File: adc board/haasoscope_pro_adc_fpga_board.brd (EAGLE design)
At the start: 224.5 x 160 mm, 573 parts, among them CN2 12Vin, IC1 ADC12DL2500ACF, IC10 TPS72325DBVR, IC13 LMH5401IRMST, IC14 LMH6401IRMZR, IC15 SN74AVC4T774PWR, IC17 DAC8562SDGSR, IC18 TLV9102IPWR, IC2 SN74AVC4T774PWR, IC21 LMH5401IRMST, IC22 TPS7A7200RGTR, IC23 TPS7A7200RGTR, IC24 TPS7A7200RGTR, IC25 TPS72325DBVR, IC26 TPS7A7200RGTR, IC27 TPS7A7200RGTR, IC28 TPS7A7200RGTR, IC29 LMH6401IRMZR, IC3 ADC122S021CIMM_NOPB, IC30 SN74AVC4T774PWR, IC33 TLV9102IPWR, IC4 TLV9102IPWR, IC5 EP4CE30F23C6N, IC6 EPCQ16ASI8N, IC7 TPS7A7200RGTR, IC8 FT232HQ, IC9 93LC56B, J1 2p-2.54, J10 8pin, J11 8pin, J13 8pin, J14 2x5, J15 test1, J2 test1, J3 2p-2.54, J30 2p-2.54, J31 2p-2.54, J32 2p-2.54, J33 2p-2.54, J34 2p-2.54, J35 2p-2.54, J36 2p-2.54, J37 2p-2.54, J39 2p-2.54, J4 2p-2.54, J40 2p-2.54, J41 2p-2.54, J42 2p-2.54, J43 2p-2.54, J44 2p-2.54, J45 2p-2.54, J46 2p-2.54, J8 8pin, K1 G6K-2F-RF-T-TR03_DC5, K2 G6K-2F-RF-T-TR03_DC5, K3 G6K-2F-RF-T-TR03_DC5, K4 G6K-2F-RF-T-TR03_DC5, K5 G6K-2F-RF-T-TR03_DC5, K6 TLP3475R_TP,F, K7 TLP3475R_TP,F, Q1 S8050, Q4 S8050, Q5 S8050, Q7 S8050, Q8 S8050, Q9 S8050, SW3 SKQGADE010, SW4 SKQGADE010, U2 ADF4350BCPZ, X1 USBC, Y2 OSCILLATORSMD-5X3, Y3 12MHz

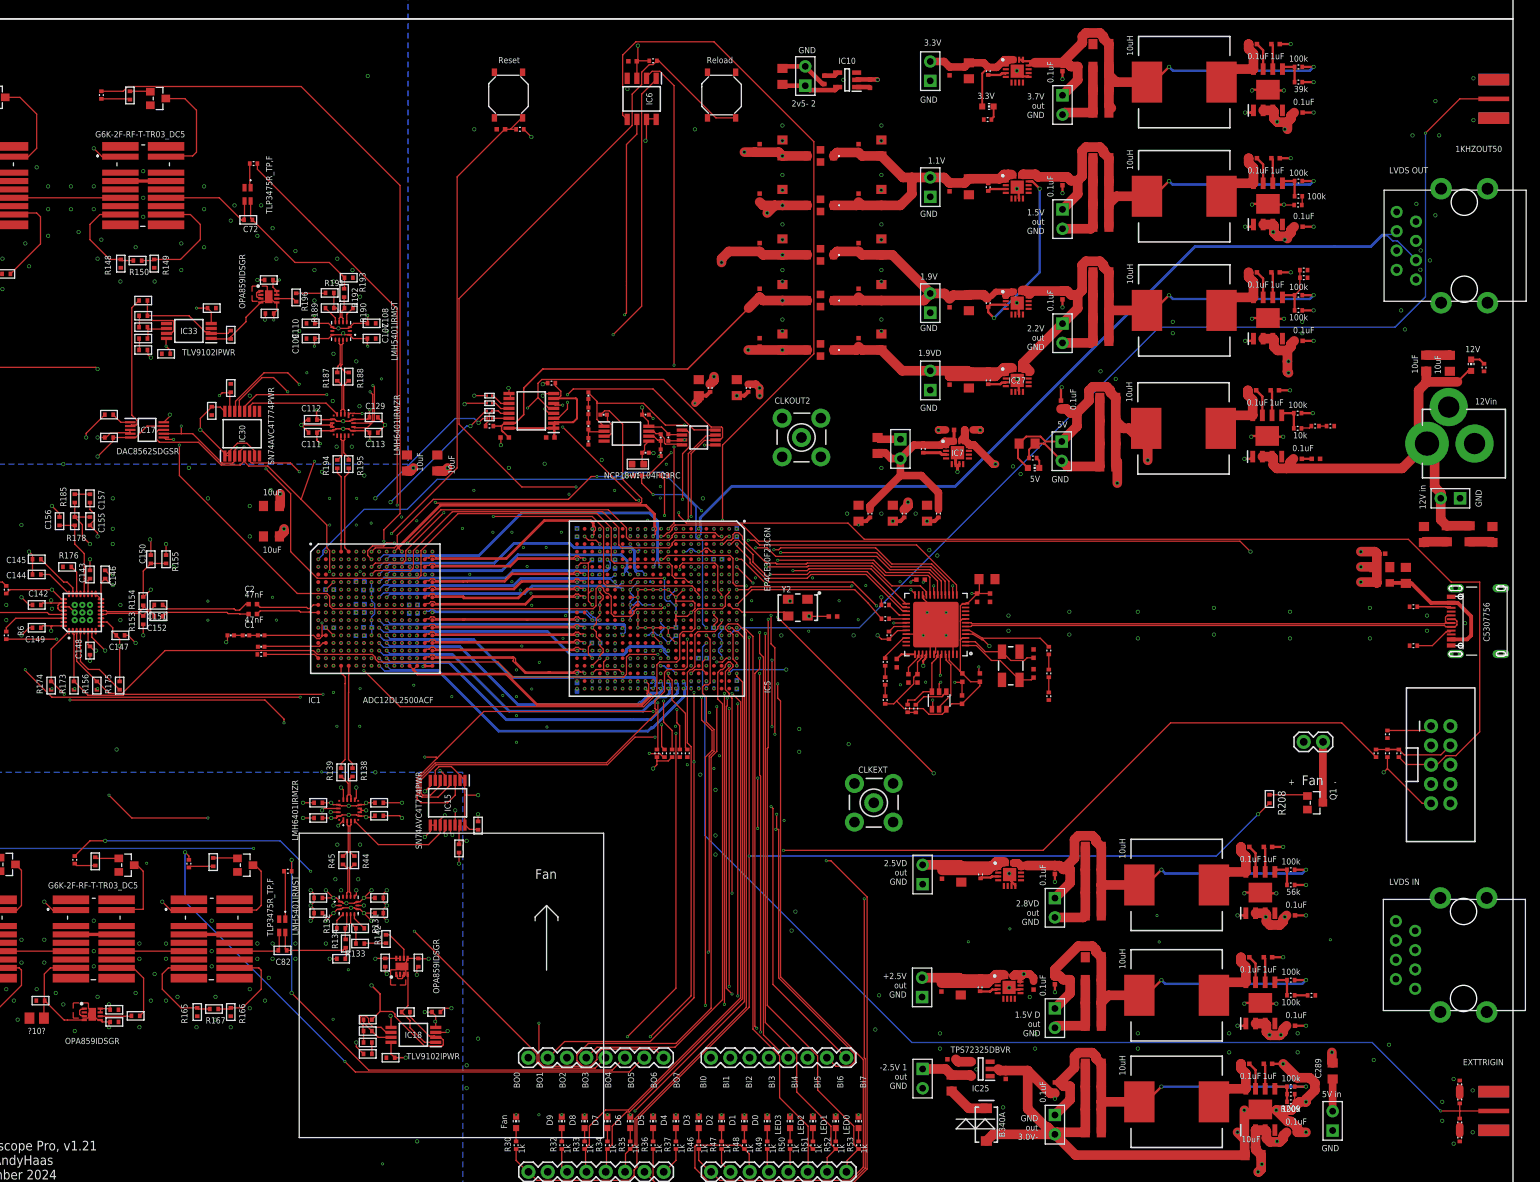
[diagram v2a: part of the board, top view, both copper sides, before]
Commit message: add more lables
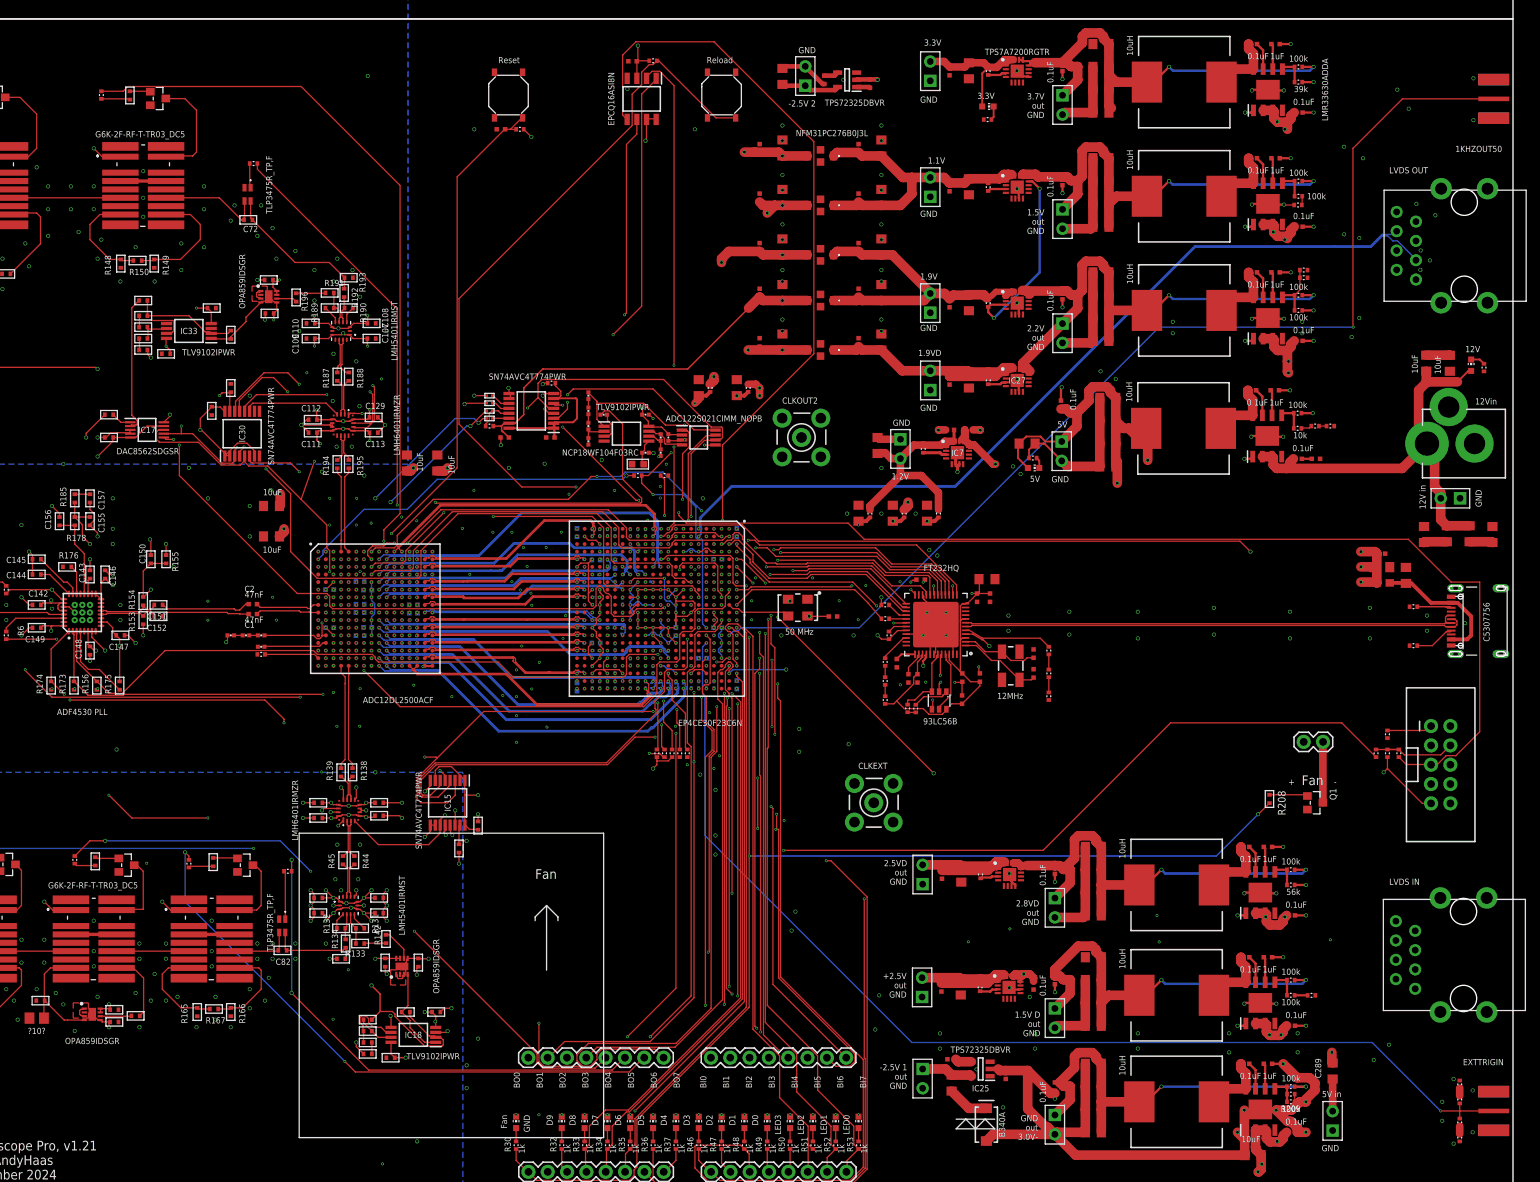
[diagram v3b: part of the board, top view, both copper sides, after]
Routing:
- net 1KHZOUT50: track 142.3 -> 143.5 mm
- net GND: vias 614 -> 617
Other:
- board text added: "-2.5V 2"
- board text added: "1.2V"
- board text added: "50 MHz"
- board text added: "ADF4530 PLL"
- board text removed: "2v5- 2"

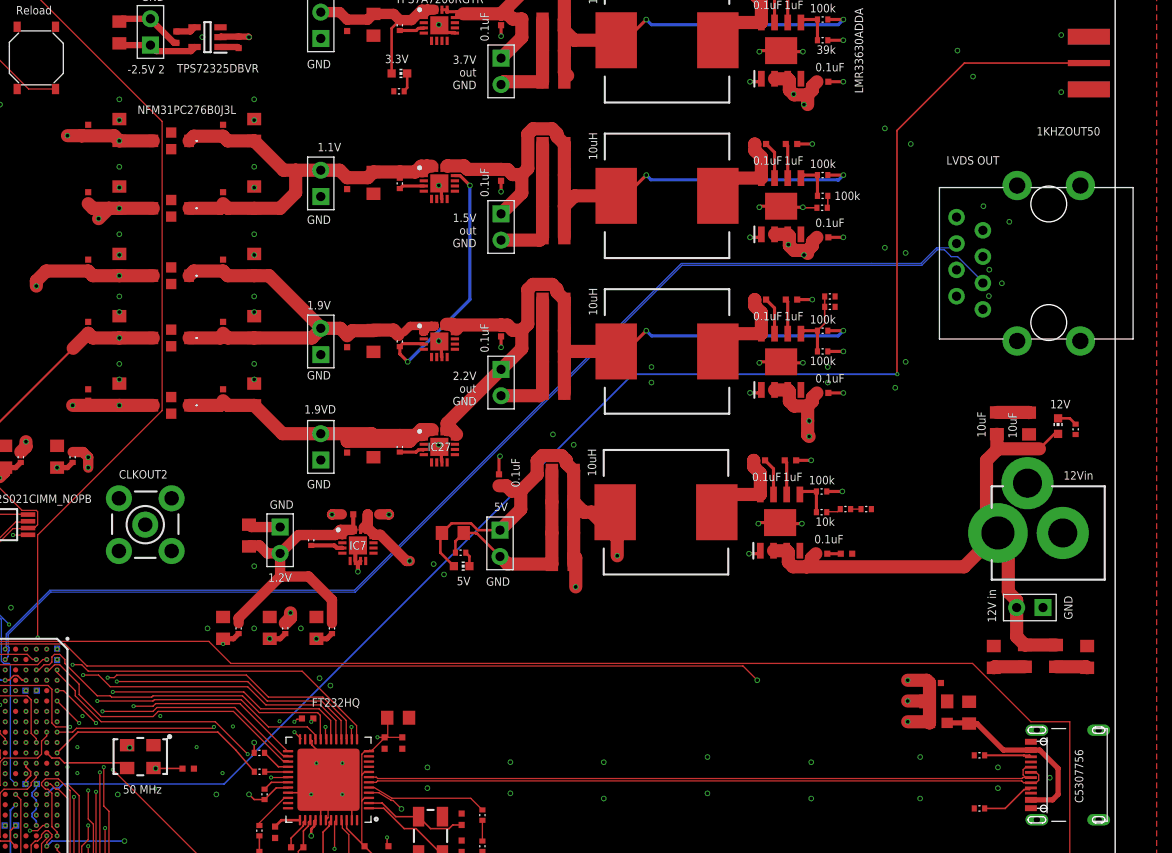
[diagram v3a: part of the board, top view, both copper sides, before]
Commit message: Add a resistor on the 50 ohm aux out line
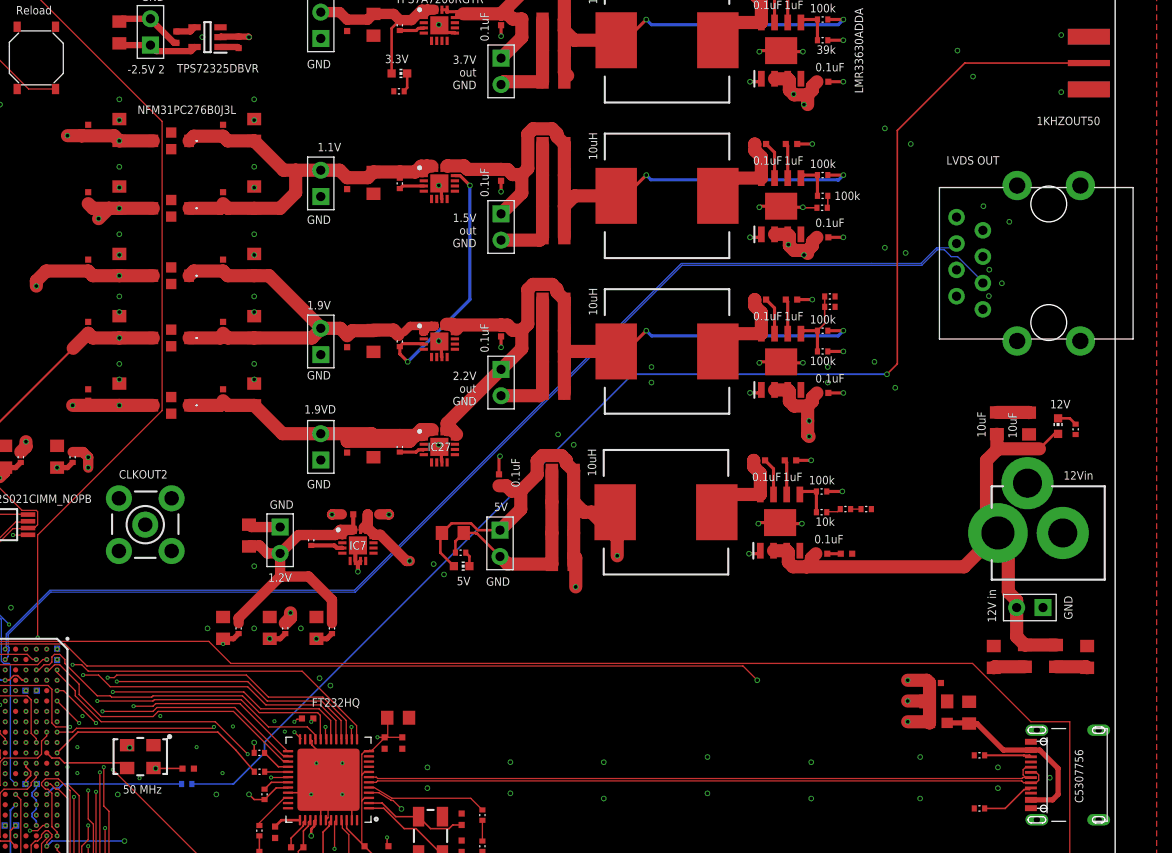
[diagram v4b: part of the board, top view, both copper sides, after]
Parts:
- added R211: 47, FlashPCB_Resistors:RES-0402
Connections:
- new net N$52: 1KHZOUT50.P, R211.P$1
- net 1KHZOUT50: now also R211.P$2; no longer 1KHZOUT50.P
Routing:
- net 1KHZOUT50: track 143.5 -> 13.4 mm, vias 2 -> 1
- net N$52: track 0.00 -> 129.0 mm, vias 0 -> 1
- net GND: vias 617 -> 618
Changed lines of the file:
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@@
 <drawing>
 <settings>
-<setting alwaysvectorfont="yes"/>
+<setting alwaysvectorfont="no"/>
 <setting verticaltext="up"/>
 </settings>
@@
 </element>
 <element name="1KHZOUT50" library="adafruit" package="SMA_EDGELAUNCH" value="50" x="224" y="146.5" smashed="yes" rot="R180">
-<attribute name="NAME" x="216.92" y="139.515" size="0.8128" layer="25"/>
+<attribute name="NAME" x="216.92" y="140.515" size="0.8128" layer="25"/>
+</element>
+<element name="R211" library="FlashPCB_Resistors" package="RES-0402" value="47" x="135" y="77" smashed="yes" rot="MR0">
+<attribute name="VALUE" x="135.77" y="78" size="0.8128" layer="22" font="vector" rot="MR0"/>
 </element>
 </elements>
@@
 <via x="135.95" y="80.55" extent="1-16" drill="0.2"/>
 <via x="138.45" y="78.05" extent="1-16" drill="0.2"/>
-<via x="131.95" y="76.55" extent="1-16" drill="0.2"/>
+<via x="130.45" y="77.55" extent="1-16" drill="0.2"/>
 <via x="139.45" y="82.55" extent="1-16" drill="0.2"/>
-<via x="143.95" y="83.05" extent="1-16" drill="0.2"/>
+<via x="143.45" y="83.05" extent="1-16" drill="0.2"/>
 <via x="24" y="125" extent="1-16" drill="0.2"/>
 <via x="24" y="122" extent="1-16" drill="0.2"/>
@@
 <via x="179.8" y="115.7" extent="1-16" drill="0.35"/>
 <via x="172.3" y="109.7" extent="1-16" drill="0.35"/>
-<via x="170.3" y="110.7" extent="1-16" drill="0.35"/>
+<via x="170.8" y="110.7" extent="1-16" drill="0.35"/>
 <via x="159.8" y="97.2" extent="1-16" drill="0.35"/>
 <via x="158.8" y="98.2" extent="1-16" drill="0.35"/>
@@
 <via x="202.3" y="128.7" extent="1-16" drill="0.35"/>
 <via x="204.3" y="128.2" extent="1-16" drill="0.35"/>
-<via x="204.3" y="117.7" extent="1-16" drill="0.35"/>
+<via x="201.3" y="117.7" extent="1-16" drill="0.35"/>
 <via x="203.3" y="115.2" extent="1-16" drill="0.35"/>
+<via x="144.45" y="82.05" extent="1-16" drill="0.2"/>
 </signal>
 <signal name="3V3" class="1">
@@
 <signal name="1KHZOUT50">
 <contactref element="IC5" pad="B15"/>
-<contactref element="1KHZOUT50" pad="P"/>
 <via x="121.5" y="76" extent="1-16" drill="0.2"/>
 <wire x1="121.5" y1="76" x2="122.093" y2="76.593" width="0.16" layer="16"/>
 <wire x1="122.093" y1="76.593" x2="122.6685875" y2="76.593" width="0.16" layer="16"/>
 <wire x1="122.6685875" y1="76.593" x2="123.0755875" y2="77" width="0.16" layer="16"/>
-<wire x1="141.305" y1="79.6968875" x2="141.305" y2="79.805" width="0.16" layer="16"/>
-<wire x1="138.6081125" y1="77" x2="141.305" y2="79.6968875" width="0.16" layer="16"/>
-<via x="203.5" y="116.5" extent="1-16" drill="0.2"/>
-<wire x1="221.968" y1="146.5" x2="209.968" y2="146.5" width="0.16" layer="1"/>
-<wire x1="209.968" y1="146.5" x2="203.468" y2="140" width="0.16" layer="1"/>
-<wire x1="203.5" y1="116.5" x2="203.468" y2="116.532" width="0.16" layer="1"/>
-<wire x1="203.468" y1="140" x2="203.468" y2="116.532" width="0.16" layer="1"/>
-<wire x1="123.0755875" y1="77" x2="138.6081125" y2="77" width="0.16" layer="16"/>
-<wire x1="141.305" y1="79.805" x2="178" y2="116.5" width="0.16" layer="16"/>
-<wire x1="178" y1="116.5" x2="203.5" y2="116.5" width="0.16" layer="16"/>
+<contactref element="R211" pad="P$2"/>
+<wire x1="123.0755875" y1="77" x2="134.5" y2="77" width="0.16" layer="16"/>
 </signal>
 <signal name="DEBUGOUT6">
@@
 <wire x1="217.5" y1="16.5" x2="217.5" y2="15.5" width="1.016" layer="1"/>
 </signal>
+<signal name="N$52">
+<contactref element="1KHZOUT50" pad="P"/>
+<contactref element="R211" pad="P$1"/>
+<wire x1="221.968" y1="146.5" x2="210" y2="146.5" width="0.16" layer="1"/>
+<wire x1="203.5" y1="117.5" x2="202.5" y2="116.5" width="0.16" layer="1"/>
+<via x="202.5" y="116.5" extent="1-16" drill="0.35"/>
+<wire x1="202.5" y1="116.5" x2="177.9755875" y2="116.5" width="0.16" layer="16"/>
+<wire x1="142.5" y1="81.0244125" x2="142.5" y2="80" width="0.16" layer="16"/>
+<wire x1="142.5" y1="80" x2="139.5" y2="77" width="0.16" layer="16"/>
+<wire x1="139.5" y1="77" x2="135.5" y2="77" width="0.16" layer="16"/>
+<wire x1="210" y1="146.5" x2="203.5" y2="140" width="0.16" layer="1"/>
+<wire x1="203.5" y1="140" x2="203.5" y2="117.5" width="0.16" layer="1"/>
+<wire x1="177.9755875" y1="116.5" x2="142.5" y2="81.0244125" width="0.16" layer="16"/>
+</signal>
 </signals>

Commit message: cleanup schematics
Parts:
- added R212: 10k, FlashPCB_Resistors:RES-0402
- added R236: 1k, FlashPCB_Resistors:RES-0402
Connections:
- new net PG12V: PS14.4, R212.P$2, R236.P$1
- net BOARDIN3: now also R236.P$2
- net VCCIO2V5: now also R212.P$1
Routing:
- net BOARDIN3: track 57.9 -> 154.9 mm, vias 3 -> 4
- net VCCIO2V5: track 48.4 -> 113.6 mm, vias 32 -> 33
- net PG12V: track 0.00 -> 9.02 mm
- net N$63: track 10.1 -> 10.7 mm

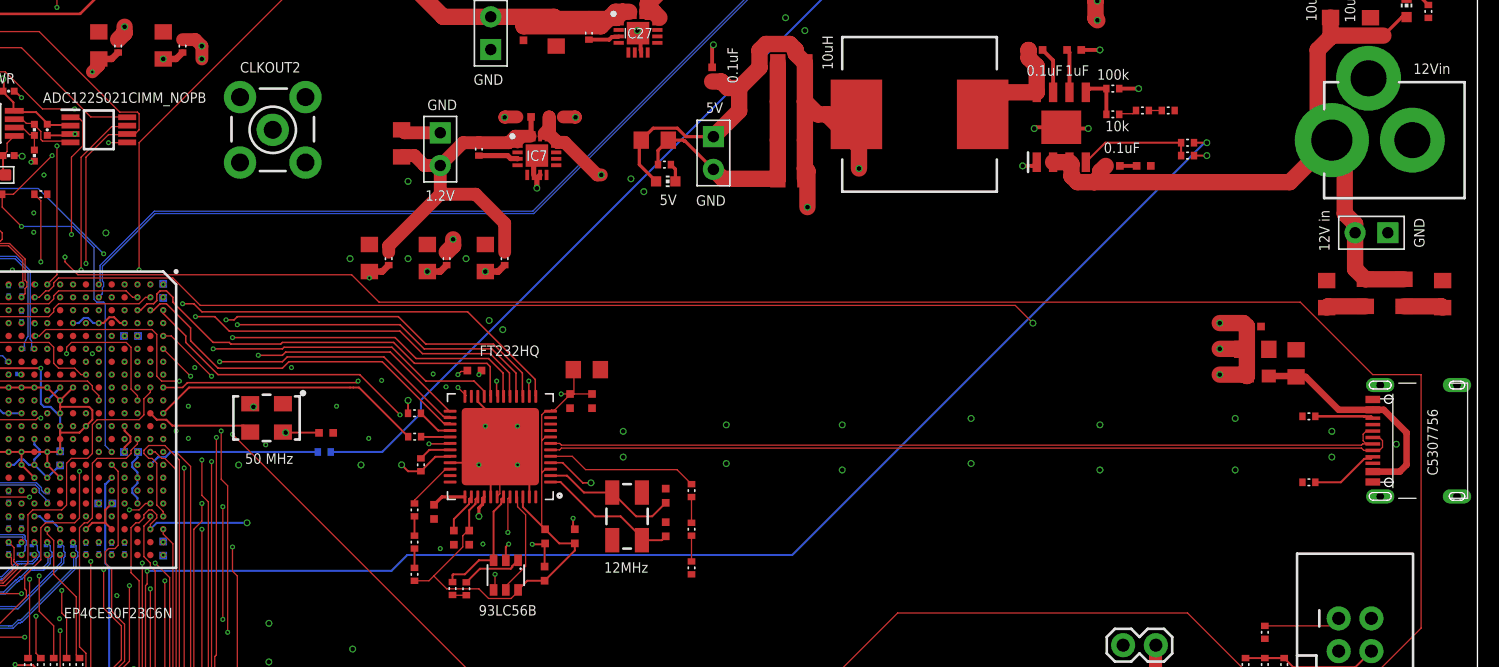
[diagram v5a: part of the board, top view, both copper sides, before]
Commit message: detect 12V and disconnect 5V from USB
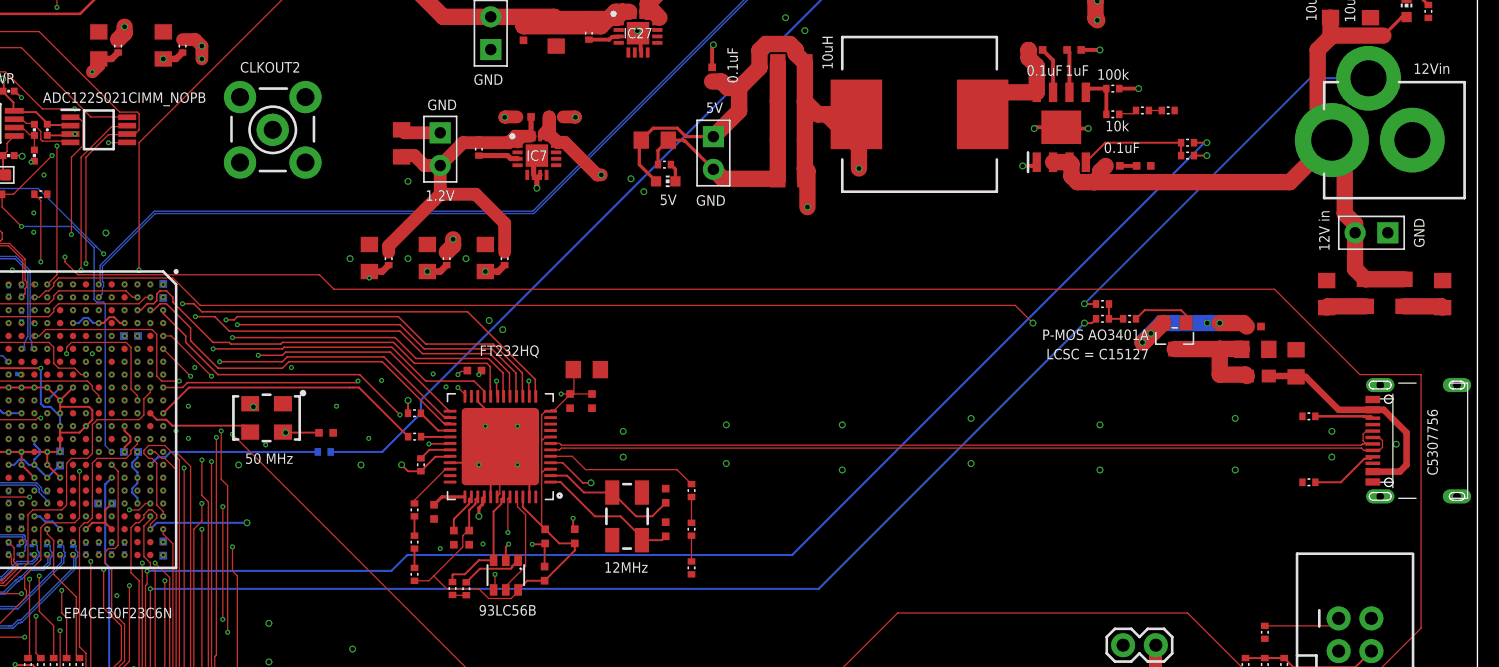
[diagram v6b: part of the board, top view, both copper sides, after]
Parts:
- added Q2: FDN340P, Seeed-Transistor:SOT-23
- added R237, R239: 10k, FlashPCB_Resistors:RES-0402
- added R238: 1k, FlashPCB_Resistors:RES-0402
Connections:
- new net 12VNOTCONNECTED: R237.P$2, R238.P$1, R239.P$1
- new net N$64: CN2.GNDBREAK, R237.P$1
- new net N$65: Q2.1, R239.P$2
- new net VBUSCLEAN: C126.2, FB2.2, Q2.3
- net 5V: now also Q2.2; no longer C126.2, FB2.2
- net BOARDIN2: now also R238.P$2
- net GND: no longer CN2.GNDBREAK
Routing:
- net BOARDIN2: track 57.8 -> 139.9 mm, vias 3 -> 4
- net N$64: track 0.00 -> 30.2 mm, vias 0 -> 1
- net VBUSCLEAN: track 0.00 -> 9.38 mm
- net N$65: track 0.00 -> 4.92 mm
- net 12VNOTCONNECTED: track 0.00 -> 2.25 mm
- net 5V: track 132.0 -> 133.1 mm, vias 25 -> 26
